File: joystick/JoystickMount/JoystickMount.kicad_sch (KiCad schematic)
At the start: 2 parts

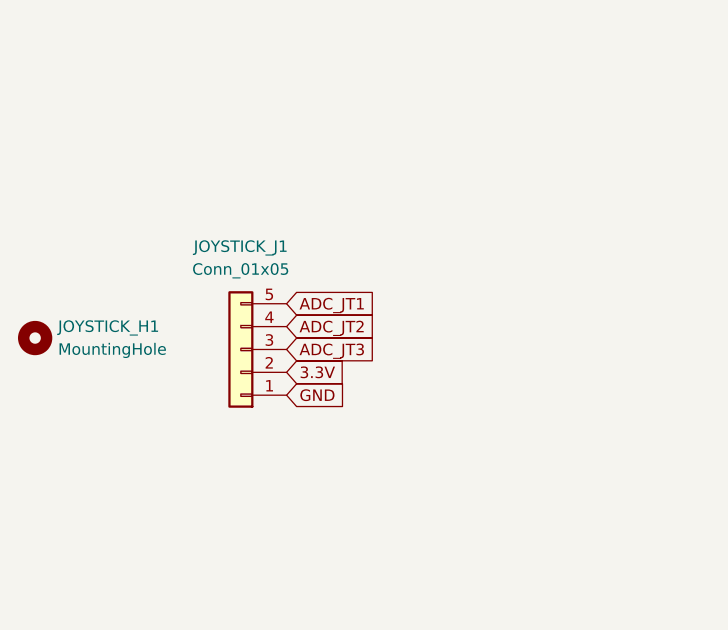
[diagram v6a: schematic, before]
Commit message: update joystick FPC to 6 pins
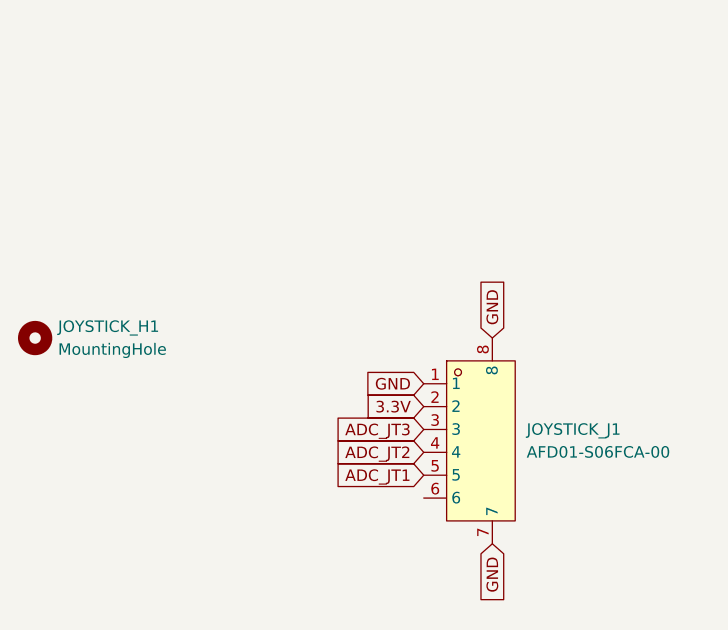
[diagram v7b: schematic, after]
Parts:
- removed JOYSTICK_J1: Conn_01x05, ErgoCai.pretty:FPC-SMD_AFC01-S05FCA-00, symbol Connector_Generic:Conn_01x05
- added JOYSTICK_J1: AFD01-S06FCA-00, ErgoCai.pretty:FPC-SMD_6P-P0.50_JS_AFD01-S06FCA-00, symbol ErgoCai:AFD01-S06FCA-00
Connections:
- net 3.3V: now also JOYSTICK_J1.2
- net ADC_JT1: now also JOYSTICK_J1.5
- net ADC_JT2: now also JOYSTICK_J1.4
- net ADC_JT3: now also JOYSTICK_J1.3
- net GND: now also JOYSTICK_J1.1, JOYSTICK_J1.7, JOYSTICK_J1.8
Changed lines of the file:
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@@
 	(generator_version "9.0")
 	(paper "A4")
+	(global_label "ADC_JT1"
+		(shape input)
+		(at 120.65 101.6 180)
+		(fields_autoplaced yes)
+		(effects
+			(font
+				(size 1.27 1.27)
+			)
+			(justify right)
+		)
+		(property "Intersheetrefs" "${INTERSHEET_REFS}"
+			(at 109.9239 101.6 0)
+			(effects
+				(font
+					(size 1.27 1.27)
+				)
+				(justify right)
+				(hide yes)
+			)
+		)
+	)
+	(global_label "GND"
+		(shape input)
+		(at 128.27 86.36 90)
+		(fields_autoplaced yes)
+		(effects
+			(font
+				(size 1.27 1.27)
+			)
+			(justify left)
+		)
+		(property "Intersheetrefs" "${INTERSHEET_REFS}"
+			(at 128.27 79.5043 90)
+			(effects
+				(font
+					(size 1.27 1.27)
+				)
+				(justify left)
+				(hide yes)
+			)
+		)
+	)
+	(global_label "ADC_JT2"
+		(shape input)
+		(at 120.65 99.06 180)
+		(fields_autoplaced yes)
+		(effects
+			(font
+				(size 1.27 1.27)
+			)
+			(justify right)
+		)
+		(property "Intersheetrefs" "${INTERSHEET_REFS}"
+			(at 109.9239 99.06 0)
+			(effects
+				(font
+					(size 1.27 1.27)
+				)
+				(justify right)
+				(hide yes)
+			)
+		)
+	)
+	(global_label "GND"
+		(shape input)
+		(at 120.65 91.44 180)
+		(fields_autoplaced yes)
+		(effects
+			(font
+				(size 1.27 1.27)
+			)
+			(justify right)
+		)
+		(property "Intersheetrefs" "${INTERSHEET_REFS}"
+			(at 113.7943 91.44 0)
+			(effects
+				(font
+					(size 1.27 1.27)
+				)
+				(justify right)
+				(hide yes)
+			)
+		)
+	)
 	(global_label "3.3V"
 		(shape input)
-		(at 105.41 90.17 0)
-		(fields_autoplaced yes)
-		(effects
-			(font
-				(size 1.27 1.27)
-			)
-			(justify left)
-		)
-		(property "Intersheetrefs" "${INTERSHEET_REFS}"
-			(at 112.5076 90.17 0)
-			(effects
-				(font
-					(size 1.27 1.27)
-				)
-				(justify left)
+		(at 120.65 93.98 180)
+		(fields_autoplaced yes)
+		(effects
+			(font
+				(size 1.27 1.27)
+			)
+			(justify right)
+		)
+		(property "Intersheetrefs" "${INTERSHEET_REFS}"
+			(at 113.5524 93.98 0)
+			(effects
+				(font
+					(size 1.27 1.27)
+				)
+				(justify right)
 				(hide yes)
 			)
@@
 	(global_label "GND"
 		(shape input)
-		(at 105.41 92.71 0)
-		(fields_autoplaced yes)
-		(effects
-			(font
-				(size 1.27 1.27)
-			)
-			(justify left)
-		)
-		(property "Intersheetrefs" "${INTERSHEET_REFS}"
-			(at 112.2657 92.71 0)
-			(effects
-				(font
-					(size 1.27 1.27)
-				)
-				(justify left)
-				(hide yes)
-			)
-		)
-	)
-	(global_label "ADC_JT1"
-		(shape input)
-		(at 105.41 82.55 0)
-		(fields_autoplaced yes)
-		(effects
-			(font
-				(size 1.27 1.27)
-			)
-			(justify left)
-		)
-		(property "Intersheetrefs" "${INTERSHEET_REFS}"
-			(at 116.1361 82.55 0)
-			(effects
-				(font
-					(size 1.27 1.27)
-				)
-				(justify left)
-				(hide yes)
-			)
-		)
-	)
-	(global_label "ADC_JT2"
-		(shape input)
-		(at 105.41 85.09 0)
-		(fields_autoplaced yes)
-		(effects
-			(font
-				(size 1.27 1.27)
-			)
-			(justify left)
-		)
-		(property "Intersheetrefs" "${INTERSHEET_REFS}"
-			(at 116.1361 85.09 0)
-			(effects
-				(font
-					(size 1.27 1.27)
-				)
-				(justify left)
+		(at 128.27 109.22 270)
+		(fields_autoplaced yes)
+		(effects
+			(font
+				(size 1.27 1.27)
+			)
+			(justify right)
+		)
+		(property "Intersheetrefs" "${INTERSHEET_REFS}"
+			(at 128.27 116.0757 90)
+			(effects
+				(font
+					(size 1.27 1.27)
+				)
+				(justify right)
 				(hide yes)
 			)
@@
 	(global_label "ADC_JT3"
 		(shape input)
-		(at 105.41 87.63 0)
-		(fields_autoplaced yes)
-		(effects
-			(font
-				(size 1.27 1.27)
-			)
-			(justify left)
-		)
-		(property "Intersheetrefs" "${INTERSHEET_REFS}"
-			(at 116.1361 87.63 0)
-			(effects
-				(font
-					(size 1.27 1.27)
-				)
-				(justify left)
+		(at 120.65 96.52 180)
+		(fields_autoplaced yes)
+		(effects
+			(font
+				(size 1.27 1.27)
+			)
+			(justify right)
+		)
+		(property "Intersheetrefs" "${INTERSHEET_REFS}"
+			(at 109.9239 96.52 0)
+			(effects
+				(font
+					(size 1.27 1.27)
+				)
+				(justify right)
 				(hide yes)
 			)
@@
 	)
 	(symbol
-		(lib_id "Connector_Generic:Conn_01x05")
-		(at 100.33 87.63 180)
+		(lib_id "ErgoCai:AFD01-S06FCA-00")
+		(at 125.73 99.06 0)
 		(unit 1)
 		(exclude_from_sim no)
@@
 		(fields_autoplaced yes)
 		(property "Reference" "JOYSTICK_J1"
-			(at 100.33 76.2 0)
-			(effects
-				(font
-					(size 1.27 1.27)
-				)
-			)
-		)
-		(property "Value" "Conn_01x05"
-			(at 100.33 78.74 0)
-			(effects
-				(font
-					(size 1.27 1.27)
-				)
-			)
-		)
-		(property "Footprint" "ErgoCai.pretty:FPC-SMD_AFC01-S05FCA-00"
-			(at 100.33 87.63 0)
-			(effects
-				(font
-					(size 1.27 1.27)
-				)
-				(hide yes)
-			)
-		)
-		(property "Datasheet" "~"
-			(at 100.33 87.63 0)
-			(effects
-				(font
-					(size 1.27 1.27)
-				)
-				(hide yes)
-			)
-		)
-		(property "Description" "Generic connector, single row, 01x05, script generated (kicad-library-utils/schlib/autogen/connector/)"
-			(at 100.33 87.63 0)
-			(effects
-				(font
-					(size 1.27 1.27)
-				)
-				(hide yes)
-			)
+			(at 132.08 96.5199 0)
+			(effects
+				(font
+					(size 1.27 1.27)
+				)
+				(justify left)
+			)
+		)
+		(property "Value" "AFD01-S06FCA-00"
+			(at 132.08 99.0599 0)
+			(effects
+				(font
+					(size 1.27 1.27)
+				)
+				(justify left)
+			)
+		)
+		(property "Footprint" "ErgoCai.pretty:FPC-SMD_6P-P0.50_JS_AFD01-S06FCA-00"
+			(at 125.73 116.84 0)
+			(effects
+				(font
+					(size 1.27 1.27)
+				)
+				(hide yes)
+			)
+		)
+		(property "Datasheet" ""
+			(at 125.73 99.06 0)
+			(effects
+				(font
+					(size 1.27 1.27)
+				)
+				(hide yes)
+			)
+		)
+		(property "Description" ""
+			(at 125.73 99.06 0)
+			(effects
+				(font
+					(size 1.27 1.27)
+				)
+				(hide yes)
+			)
+		)
+		(property "LCSC Part" "C18198574"
+			(at 125.73 119.38 0)
+			(effects
+				(font
+					(size 1.27 1.27)
+				)
+				(hide yes)
+			)
+		)
+		(pin "3"
 		)
 		(pin "4"
 		)
+		(pin "1"
+		)
+		(pin "2"
+		)
+		(pin "8"
+		)
+		(pin "7"
+		)
 		(pin "5"
 		)
-		(pin "2"
-		)
-		(pin "3"
-		)
-		(pin "1"
+		(pin "6"
 		)
 		(instances
-			(project "JoystickMount"
+			(project ""
 				(path "/a3bb8e3e-5002-46e5-9310-dabcf88c147f"
 					(reference "JOYSTICK_J1")

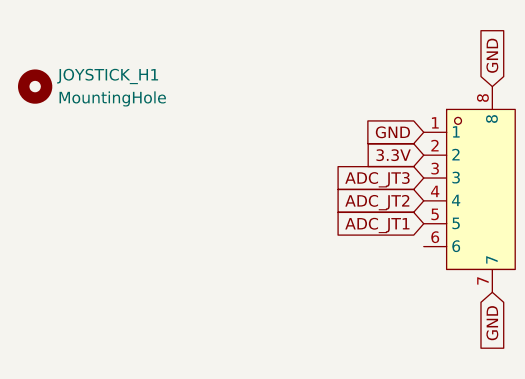
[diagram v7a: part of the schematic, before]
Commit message: add joystick_fpc_hole
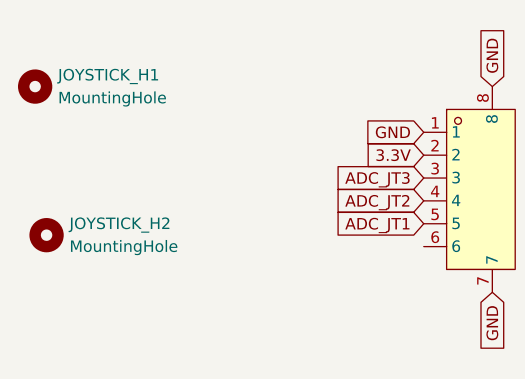
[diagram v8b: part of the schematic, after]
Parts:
- added JOYSTICK_H2: MountingHole, ErgoCai.pretty:joystick_fpc_hole, symbol Mechanical:MountingHole
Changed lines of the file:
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@@
+	)
+	(symbol
+		(lib_id "Mechanical:MountingHole")
+		(at 78.74 102.87 0)
+		(unit 1)
+		(exclude_from_sim no)
+		(in_bom no)
+		(on_board yes)
+		(dnp no)
+		(fields_autoplaced yes)
+		(property "Reference" "JOYSTICK_H2"
+			(at 81.28 101.5999 0)
+			(effects
+				(font
+					(size 1.27 1.27)
+				)
+				(justify left)
+			)
+		)
+		(property "Value" "MountingHole"
+			(at 81.28 104.1399 0)
+			(effects
+				(font
+					(size 1.27 1.27)
+				)
+				(justify left)
+			)
+		)
+		(property "Footprint" "ErgoCai.pretty:joystick_fpc_hole"
+			(at 78.74 102.87 0)
+			(effects
+				(font
+					(size 1.27 1.27)
+				)
+				(hide yes)
+			)
+		)
+		(property "Datasheet" "~"
+			(at 78.74 102.87 0)
+			(effects
+				(font
+					(size 1.27 1.27)
+				)
+				(hide yes)
+			)
+		)
+		(property "Description" "Mounting Hole without connection"
+			(at 78.74 102.87 0)
+			(effects
+				(font
+					(size 1.27 1.27)
+				)
+				(hide yes)
+			)
+		)
+		(instances
+			(project "JoystickMount"
+				(path "/a3bb8e3e-5002-46e5-9310-dabcf88c147f"
+					(reference "JOYSTICK_H2")
+					(unit 1)
+				)
+			)
+		)
 	)
 	(symbol
@@
 		)
 		(instances
-			(project ""
+			(project "JoystickMount"
 				(path "/a3bb8e3e-5002-46e5-9310-dabcf88c147f"
 					(reference "JOYSTICK_J1")
@@
 		)
 		(instances
-			(project ""
+			(project "JoystickMount"
 				(path "/a3bb8e3e-5002-46e5-9310-dabcf88c147f"
 					(reference "JOYSTICK_H1")
